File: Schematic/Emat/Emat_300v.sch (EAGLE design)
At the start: 45 parts, among them IC1 UC3843N, Q1 BSS138, Q2 IRF640IW220B

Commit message: Further work on schematic.
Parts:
- added C14: 1.2nF 630V K78-2, rcl:C-EU150-064X183
- added C15: 220pF 1000V, rcl:C-EU075-042X103
- added C16, C17: 330nF 630V K73-17, rcl:C-EU225-062X268
- added C19: 47uF 450V, rcl:CPOL-USE7.5-18
- added D7: MUR4100, diode:DIODE-DO201-15
- added J1, J2: PIN1-2, con-faston:PIN1-2
- added R21, R22: 100, resistor:R-US_R2512
- added R23, R24: 51, resistor:R-US_R1206
- added T1: EFD25-2, trafo:EFD25-2
- R5: value 4.7K -> 3.6K
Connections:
- removed net N$2: R1.2
- new net N$18: J1.1, OK2.A
- new net N$19: J2.1, OK2.C
- new net N$20: Q2.D, R21.2, R22.2, T1.P1
- new net N$21: C14.1, R21.1, R22.1
- new net N$22: C15.2, D7.A, T1.S1
- new net N$24: R23.1, R24.2
- new net N$25: C15.1, R23.2
- new net V+: C16.1, C17.1, C19.+, D1.C, D7.C, R1.2, R24.1
- new net V-: C16.2, C17.2, C19.-, D2.A, T1.S2
- net +12V: now also T1.P2
- net GND: now also C14.2
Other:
- note added: "Core Size: EFD25/13/9 Core Material: N87 Bobbin: EFD25/13/9 Gap: 145.47 um +---------------------------------+ | Winding # 1 | Wire: AWG24 | Number of Turns: 10 +---------------------------------+ | Winding # 2 | Wire: AWG25 | Number of Turns: 35 +---------------------------------+"
- moved on the sheet: C10, C11, C12, C13, C9, L2, R10, R11, R12, R13, R14, R15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

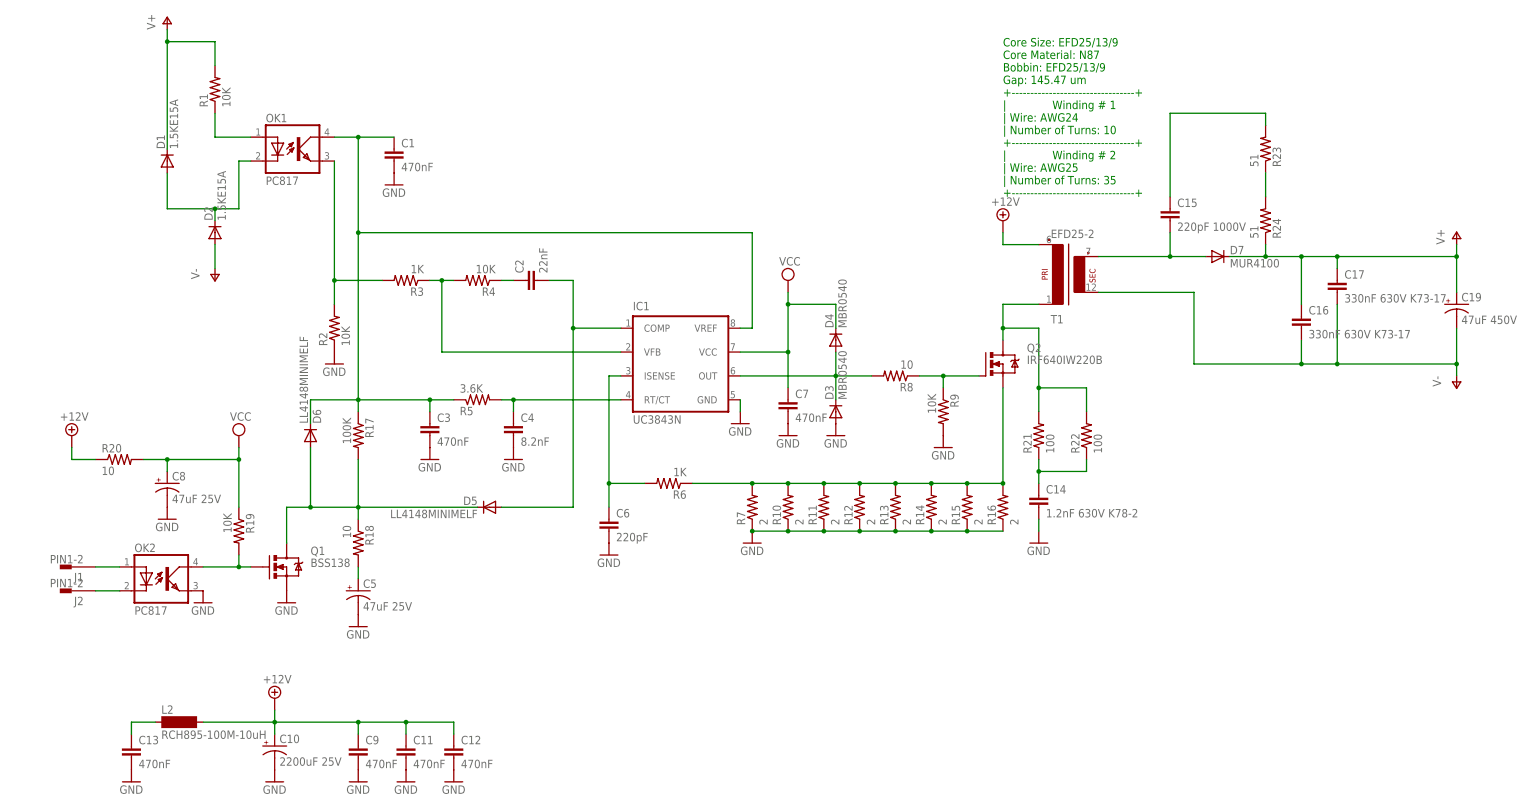
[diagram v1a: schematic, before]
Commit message: 300V pcb done
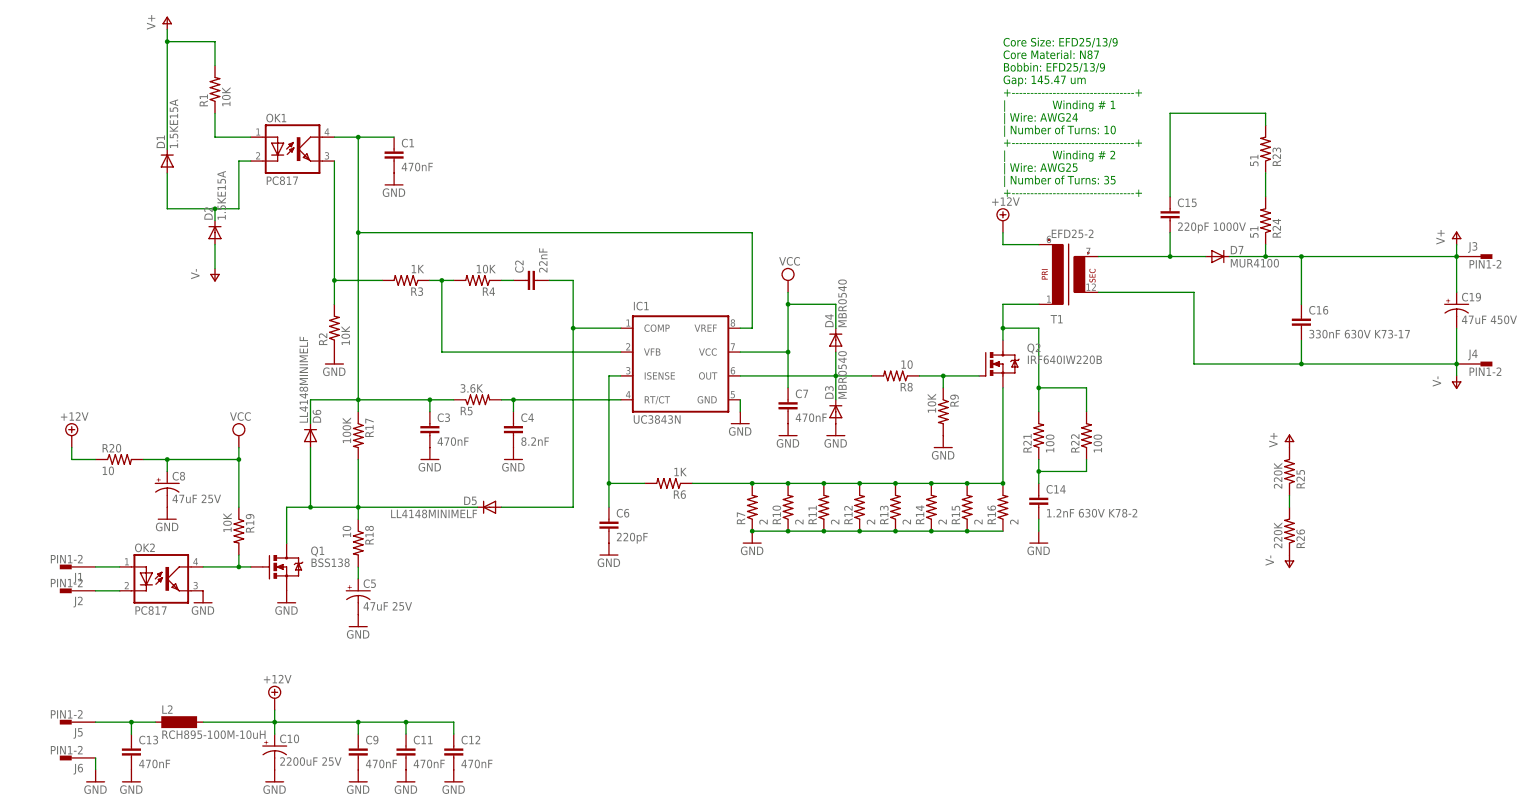
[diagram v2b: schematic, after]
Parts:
- removed C17: 330nF 630V K73-17, rcl:C-EU225-062X268
- added J3, J4, J5, J6: PIN1-2, con-faston:PIN1-2
- added R25, R26: 220K, resistor:R-US_R1206
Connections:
- new net N$2: R25.1, R26.2
- net GND: now also J6.1
- net N$16: now also J5.1
- net V+: now also J3.1, R25.2; no longer C17.1
- net V-: now also J4.1, R26.1; no longer C17.2
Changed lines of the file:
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@@
 <part name="R24" library="resistor" deviceset="R-US_" device="R1206" value="51"/>
 <part name="C16" library="rcl" deviceset="C-EU" device="225-062X268" value="330nF 630V K73-17"/>
-<part name="C17" library="rcl" deviceset="C-EU" device="225-062X268" value="330nF 630V K73-17"/>
 <part name="C19" library="rcl" deviceset="CPOL-US" device="E7.5-18" value="47uF 450V"/>
 <part name="P+1" library="supply1" deviceset="V+" device=""/>
@@
 <part name="P-2" library="supply1" deviceset="V-" device=""/>
 <part name="T1" library="trafo" deviceset="EFD25-2" device=""/>
+<part name="J3" library="con-faston" deviceset="PIN1-2" device=""/>
+<part name="J4" library="con-faston" deviceset="PIN1-2" device=""/>
+<part name="J5" library="con-faston" deviceset="PIN1-2" device=""/>
+<part name="J6" library="con-faston" deviceset="PIN1-2" device=""/>
+<part name="GND21" library="SparkFun-Aesthetics" deviceset="GND" device=""/>
+<part name="R25" library="resistor" deviceset="R-US_" device="R1206" value="220K"/>
+<part name="R26" library="resistor" deviceset="R-US_" device="R1206" value="220K"/>
+<part name="P-3" library="supply1" deviceset="V-" device=""/>
+<part name="P+3" library="supply1" deviceset="V+" device=""/>
 </parts>
 <sheets>
@@
 <instance part="R24" gate="G$1" x="226.06" y="66.04" rot="MR90"/>
 <instance part="C16" gate="G$1" x="233.68" y="45.72"/>
-<instance part="C17" gate="G$1" x="241.3" y="53.34"/>
 <instance part="C19" gate="G$1" x="266.7" y="48.26"/>
 <instance part="P+1" gate="1" x="266.7" y="63.5"/>
@@
 <instance part="P-2" gate="1" x="266.7" y="30.48"/>
 <instance part="T1" gate="G$1" x="182.88" y="53.34" rot="MR180"/>
+<instance part="J3" gate="G$1" x="271.78" y="58.42"/>
+<instance part="J4" gate="G$1" x="271.78" y="35.56"/>
+<instance part="J5" gate="G$1" x="-27.94" y="-40.64" rot="R180"/>
+<instance part="J6" gate="G$1" x="-27.94" y="-48.26" rot="R180"/>
+<instance part="GND21" gate="1" x="-22.86" y="-53.34"/>
+<instance part="R25" gate="G$1" x="231.14" y="12.7" rot="MR90"/>
+<instance part="R26" gate="G$1" x="231.14" y="0" rot="MR90"/>
+<instance part="P-3" gate="1" x="231.14" y="-7.62"/>
+<instance part="P+3" gate="1" x="231.14" y="20.32"/>
 </instances>
 <busses>
@@
 <pinref part="GND20" gate="1" pin="GND"/>
 <wire x1="177.8" y1="0" x2="177.8" y2="2.54" width="0.1524" layer="91"/>
+</segment>
+<segment>
+<pinref part="J6" gate="G$1" pin="1"/>
+<pinref part="GND21" gate="1" pin="GND"/>
+<wire x1="-22.86" y1="-50.8" x2="-22.86" y2="-48.26" width="0.1524" layer="91"/>
 </segment>
 </net>
@@
 <wire x1="-10.16" y1="-40.64" x2="-15.24" y2="-40.64" width="0.1524" layer="91"/>
 <wire x1="-15.24" y1="-40.64" x2="-15.24" y2="-43.18" width="0.1524" layer="91"/>
+<pinref part="J5" gate="G$1" pin="1"/>
+<wire x1="-22.86" y1="-40.64" x2="-15.24" y2="-40.64" width="0.1524" layer="91"/>
+<junction x="-15.24" y="-40.64"/>
 </segment>
 </net>
@@
 <pinref part="C16" gate="G$1" pin="2"/>
 <wire x1="233.68" y1="40.64" x2="233.68" y2="35.56" width="0.1524" layer="91"/>
-<wire x1="233.68" y1="35.56" x2="241.3" y2="35.56" width="0.1524" layer="91"/>
-<wire x1="241.3" y1="35.56" x2="266.7" y2="35.56" width="0.1524" layer="91"/>
+<wire x1="233.68" y1="35.56" x2="266.7" y2="35.56" width="0.1524" layer="91"/>
 <wire x1="266.7" y1="35.56" x2="266.7" y2="43.18" width="0.1524" layer="91"/>
 <wire x1="210.82" y1="50.8" x2="210.82" y2="35.56" width="0.1524" layer="91"/>
 <wire x1="210.82" y1="35.56" x2="233.68" y2="35.56" width="0.1524" layer="91"/>
 <junction x="233.68" y="35.56"/>
-<junction x="241.3" y="35.56"/>
-<pinref part="C17" gate="G$1" pin="2"/>
-<wire x1="241.3" y1="48.26" x2="241.3" y2="35.56" width="0.1524" layer="91"/>
 <pinref part="C19" gate="G$1" pin="-"/>
 <pinref part="P-2" gate="1" pin="V-"/>
@@
 <pinref part="T1" gate="G$1" pin="S2"/>
 <wire x1="190.5" y1="50.8" x2="210.82" y2="50.8" width="0.1524" layer="91"/>
+<pinref part="J4" gate="G$1" pin="1"/>
 </segment>
 <segment>
@@
 <pinref part="P-1" gate="1" pin="V-"/>
 <wire x1="2.54" y1="60.96" x2="2.54" y2="55.88" width="0.1524" layer="91"/>
+</segment>
+<segment>
+<pinref part="R26" gate="G$1" pin="1"/>
+<pinref part="P-3" gate="1" pin="V-"/>
 </segment>
 </net>
@@
 <wire x1="226.06" y1="58.42" x2="226.06" y2="60.96" width="0.1524" layer="91"/>
 <pinref part="D7" gate="G$1" pin="C"/>
-<pinref part="C17" gate="G$1" pin="1"/>
 <wire x1="226.06" y1="58.42" x2="233.68" y2="58.42" width="0.1524" layer="91"/>
-<wire x1="233.68" y1="58.42" x2="241.3" y2="58.42" width="0.1524" layer="91"/>
-<wire x1="241.3" y1="58.42" x2="241.3" y2="55.88" width="0.1524" layer="91"/>
 <wire x1="266.7" y1="50.8" x2="266.7" y2="58.42" width="0.1524" layer="91"/>
-<wire x1="266.7" y1="58.42" x2="241.3" y2="58.42" width="0.1524" layer="91"/>
-<junction x="241.3" y="58.42"/>
+<wire x1="266.7" y1="58.42" x2="233.68" y2="58.42" width="0.1524" layer="91"/>
 <pinref part="C16" gate="G$1" pin="1"/>
 <wire x1="233.68" y1="48.26" x2="233.68" y2="58.42" width="0.1524" layer="91"/>
@@
 <wire x1="266.7" y1="60.96" x2="266.7" y2="58.42" width="0.1524" layer="91"/>
 <junction x="266.7" y="58.42"/>
+<pinref part="J3" gate="G$1" pin="1"/>
 </segment>
 <segment>
@@
 <pinref part="D1" gate="G$1" pin="C"/>
 </segment>
-</net>
+<segment>
+<pinref part="R25" gate="G$1" pin="2"/>
+<pinref part="P+3" gate="1" pin="V+"/>
+</segment>
+</net>
+<net name="N$2" class="0">
+<segment>
+<pinref part="R25" gate="G$1" pin="1"/>
+<pinref part="R26" gate="G$1" pin="2"/>
+<wire x1="231.14" y1="5.08" x2="231.14" y2="7.62" width="0.1524" layer="91"/>
+</segment>
+</net>

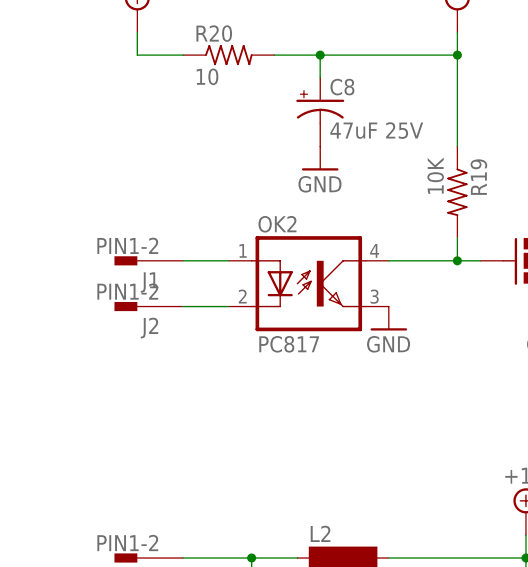
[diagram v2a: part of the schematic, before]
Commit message: Add resistor before opto-coupler.
To enable direct controll from STM32.
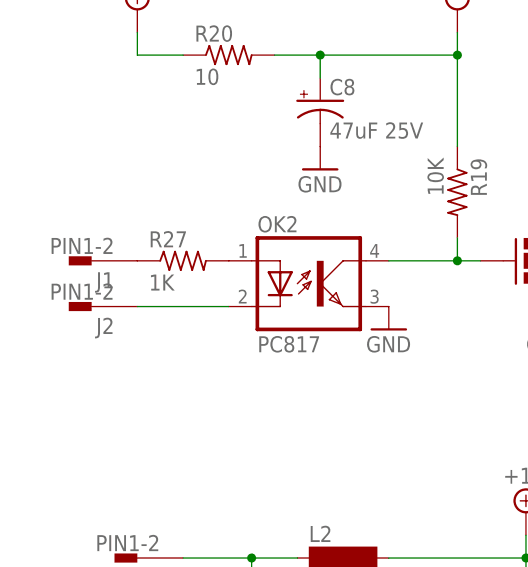
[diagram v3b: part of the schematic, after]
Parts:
- added R27: 1K, resistor:R-US_R1206
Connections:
- new net N$23: J1.1, R27.1
- net N$18: now also R27.2; no longer J1.1
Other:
- moved on the sheet: J1, J2
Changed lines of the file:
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@@
 <part name="P-3" library="supply1" deviceset="V-" device=""/>
 <part name="P+3" library="supply1" deviceset="V+" device=""/>
+<part name="R27" library="resistor" deviceset="R-US_" device="R1206" value="1K"/>
 </parts>
 <sheets>
@@
 <instance part="C13" gate="G$1" x="-15.24" y="-45.72"/>
 <instance part="GND19" gate="1" x="-15.24" y="-53.34"/>
-<instance part="J1" gate="G$1" x="-27.94" y="-7.62" rot="R180"/>
-<instance part="J2" gate="G$1" x="-27.94" y="-12.7" rot="R180"/>
+<instance part="J1" gate="G$1" x="-33.02" y="-7.62" rot="R180"/>
+<instance part="J2" gate="G$1" x="-33.02" y="-12.7" rot="R180"/>
 <instance part="R21" gate="G$1" x="177.8" y="20.32" rot="R90"/>
 <instance part="R22" gate="G$1" x="187.96" y="20.32" rot="R90"/>
@@
 <instance part="P-3" gate="1" x="231.14" y="-7.62"/>
 <instance part="P+3" gate="1" x="231.14" y="20.32"/>
+<instance part="R27" gate="G$1" x="-22.86" y="-7.62"/>
 </instances>
 <busses>
@@
 </segment>
 </net>
-<net name="N$18" class="0">
-<segment>
-<pinref part="OK2" gate="A" pin="A"/>
-<pinref part="J1" gate="G$1" pin="1"/>
-<wire x1="-22.86" y1="-7.62" x2="-17.78" y2="-7.62" width="0.1524" layer="91"/>
-</segment>
-</net>
 <net name="N$19" class="0">
 <segment>
 <pinref part="OK2" gate="A" pin="C"/>
 <pinref part="J2" gate="G$1" pin="1"/>
-<wire x1="-22.86" y1="-12.7" x2="-17.78" y2="-12.7" width="0.1524" layer="91"/>
+<wire x1="-27.94" y1="-12.7" x2="-17.78" y2="-12.7" width="0.1524" layer="91"/>
 </segment>
 </net>
@@
 </segment>
 </net>
+<net name="N$18" class="0">
+<segment>
+<pinref part="OK2" gate="A" pin="A"/>
+<pinref part="R27" gate="G$1" pin="2"/>
+</segment>
+</net>
+<net name="N$23" class="0">
+<segment>
+<pinref part="R27" gate="G$1" pin="1"/>
+<pinref part="J1" gate="G$1" pin="1"/>
+</segment>
+</net>

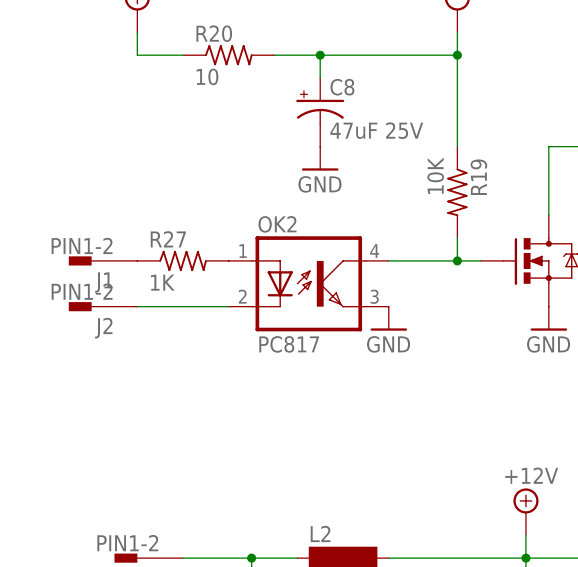
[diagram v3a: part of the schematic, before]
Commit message: Add HV On Off command.
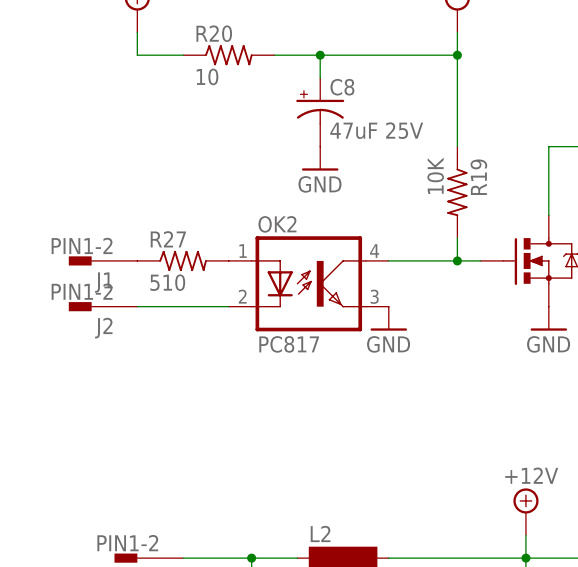
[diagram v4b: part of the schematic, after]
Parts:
- R27: value 1K -> 510
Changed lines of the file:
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@@
 <part name="P-3" library="supply1" deviceset="V-" device=""/>
 <part name="P+3" library="supply1" deviceset="V+" device=""/>
-<part name="R27" library="resistor" deviceset="R-US_" device="R1206" value="1K"/>
+<part name="R27" library="resistor" deviceset="R-US_" device="R1206" value="510"/>
 </parts>
 <sheets>

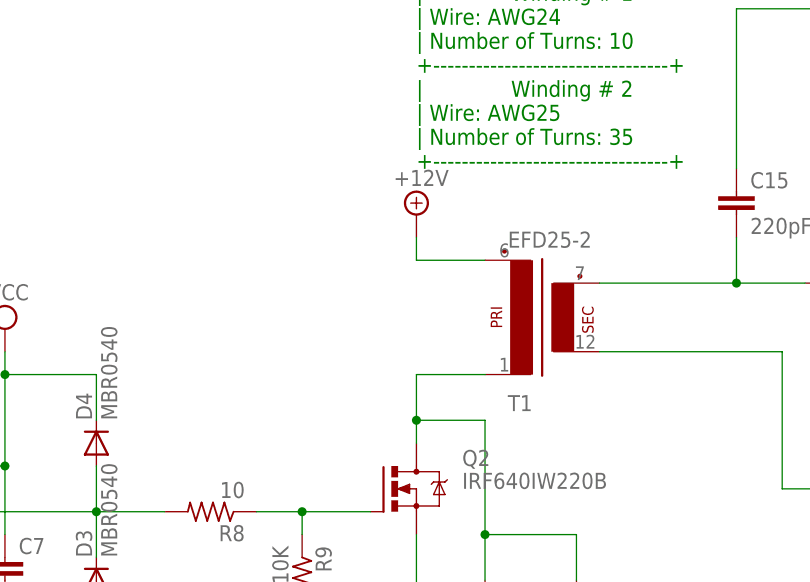
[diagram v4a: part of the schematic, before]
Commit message: Fix transformer wiring.
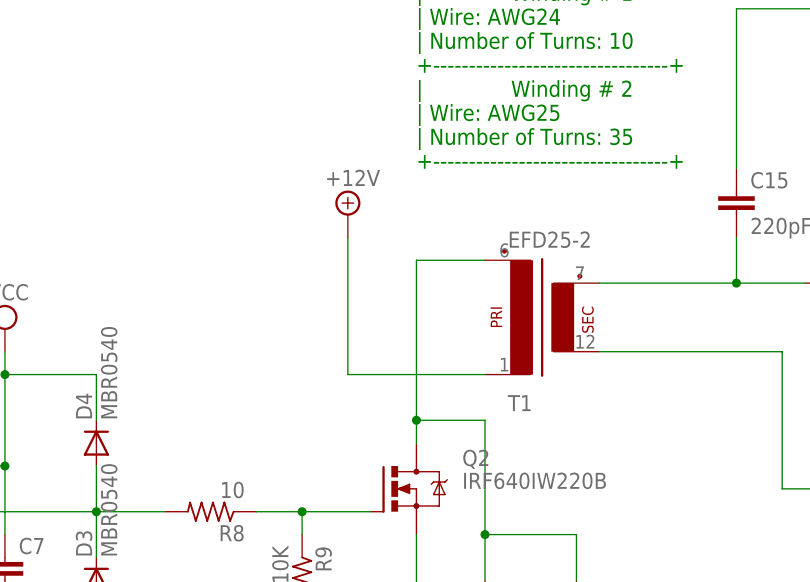
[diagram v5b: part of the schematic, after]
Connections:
- net +12V: now also T1.P1; no longer T1.P2
- net N$20: now also T1.P2; no longer T1.P1
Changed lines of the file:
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@@
 <instance part="C14" gate="G$1" x="177.8" y="7.62"/>
 <instance part="GND20" gate="1" x="177.8" y="-2.54"/>
-<instance part="SUPPLY5" gate="+12V" x="170.18" y="66.04"/>
+<instance part="SUPPLY5" gate="+12V" x="162.56" y="66.04"/>
 <instance part="D7" gate="G$1" x="215.9" y="58.42"/>
 <instance part="C15" gate="G$1" x="205.74" y="68.58"/>
@@
 </segment>
 <segment>
+<pinref part="T1" gate="G$1" pin="P1"/>
 <pinref part="SUPPLY5" gate="+12V" pin="+12V"/>
-<wire x1="170.18" y1="63.5" x2="170.18" y2="60.96" width="0.1524" layer="91"/>
-<pinref part="T1" gate="G$1" pin="P2"/>
-<wire x1="177.8" y1="60.96" x2="170.18" y2="60.96" width="0.1524" layer="91"/>
+<wire x1="177.8" y1="48.26" x2="162.56" y2="48.26" width="0.1524" layer="91"/>
+<wire x1="162.56" y1="48.26" x2="162.56" y2="63.5" width="0.1524" layer="91"/>
 </segment>
 </net>
@@
 <pinref part="Q2" gate="G$1" pin="D"/>
 <wire x1="170.18" y1="40.64" x2="170.18" y2="43.18" width="0.1524" layer="91"/>
-<wire x1="170.18" y1="43.18" x2="170.18" y2="48.26" width="0.1524" layer="91"/>
 <pinref part="R21" gate="G$1" pin="2"/>
 <wire x1="170.18" y1="43.18" x2="177.8" y2="43.18" width="0.1524" layer="91"/>
@@
 <junction x="177.8" y="30.48"/>
 <junction x="170.18" y="43.18"/>
-<pinref part="T1" gate="G$1" pin="P1"/>
-<wire x1="177.8" y1="48.26" x2="170.18" y2="48.26" width="0.1524" layer="91"/>
-</segment>
-</net>
+<pinref part="T1" gate="G$1" pin="P2"/>
+<wire x1="177.8" y1="60.96" x2="170.18" y2="60.96" width="0.1524" layer="91"/>
+<wire x1="170.18" y1="60.96" x2="170.18" y2="48.26" width="0.1524" layer="91"/>
+<wire x1="170.18" y1="45.72" x2="170.18" y2="43.18" width="0.1524" layer="91"/>
+<wire x1="170.18" y1="48.26" x2="170.18" y2="45.72" width="0.1524" layer="91"/>
+</segment>
+</net>
